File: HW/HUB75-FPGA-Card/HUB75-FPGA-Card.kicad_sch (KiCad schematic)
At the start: 0 parts

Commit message: add usb audio implementation
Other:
- added sheet USB Audio (USBAudio.kicad_sch)
- sheet FPGA ports: added B1, B2, B3, B4, BLANK, CLKOUT, CLK_12MHZ, CLK_60MHZ, D0, D1, D2, D3, D4, D5, D6, D7, G1, G2, G3, G4, LAT, R1, R2, R3, R4, ROW_CLK, ROW_DATA, STRIP1, STRIP2, STRIP3, STRIP4, ~{OE}, ~{RD}, ~{RXF}, ~{TXE}, ~{WR}; removed none
- sheet FTDI ports: added none; removed VIN_5V
- sheet Hub75 ports: added B1, B2, B3, B4, BLANK, CLKOUT, G1, G2, G3, G4, LAT, R1, R2, R3, R4, ROW_CLK, ROW_DATA, STRIP1, STRIP2, STRIP3, STRIP4; removed none

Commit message: rename Hub75 schematic page to LevelShifters
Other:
- sheet Hub75 renamed Level Shifters
- sheet Level Shifters: file Hub75.kicad_sch -> LevelShifters.kicad_sch
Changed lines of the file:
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@@
     (stroke (width 0.1524) (type solid))
     (fill (color 0 0 0 0.0000))
-    (property "Sheetname" "Hub75" (at 168.91 50.0884 0)
+    (property "Sheetname" "Level Shifters" (at 168.91 50.0884 0)
       (effects (font (size 1.27 1.27)) (justify left bottom))
     )
-    (property "Sheetfile" "Hub75.kicad_sch" (at 168.91 114.8846 0)
+    (property "Sheetfile" "LevelShifters.kicad_sch" (at 168.91 114.8846 0)
       (effects (font (size 1.27 1.27)) (justify left top))
     )

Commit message: finish up schematic and begin routing
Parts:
- added H1, H2, H3, H4: MountingHole, MountingHole:MountingHole_3.2mm_M3, symbol Mechanical:MountingHole
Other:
- removed sheet Power
- added sheet USB Hub (USBHub.kicad_sch)

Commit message: saving hardware progress
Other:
- added sheet MCU (MCU.kicad_sch)
- sheet USB Hub ports: added USB_MCU_D+, USB_MCU_D-; removed none

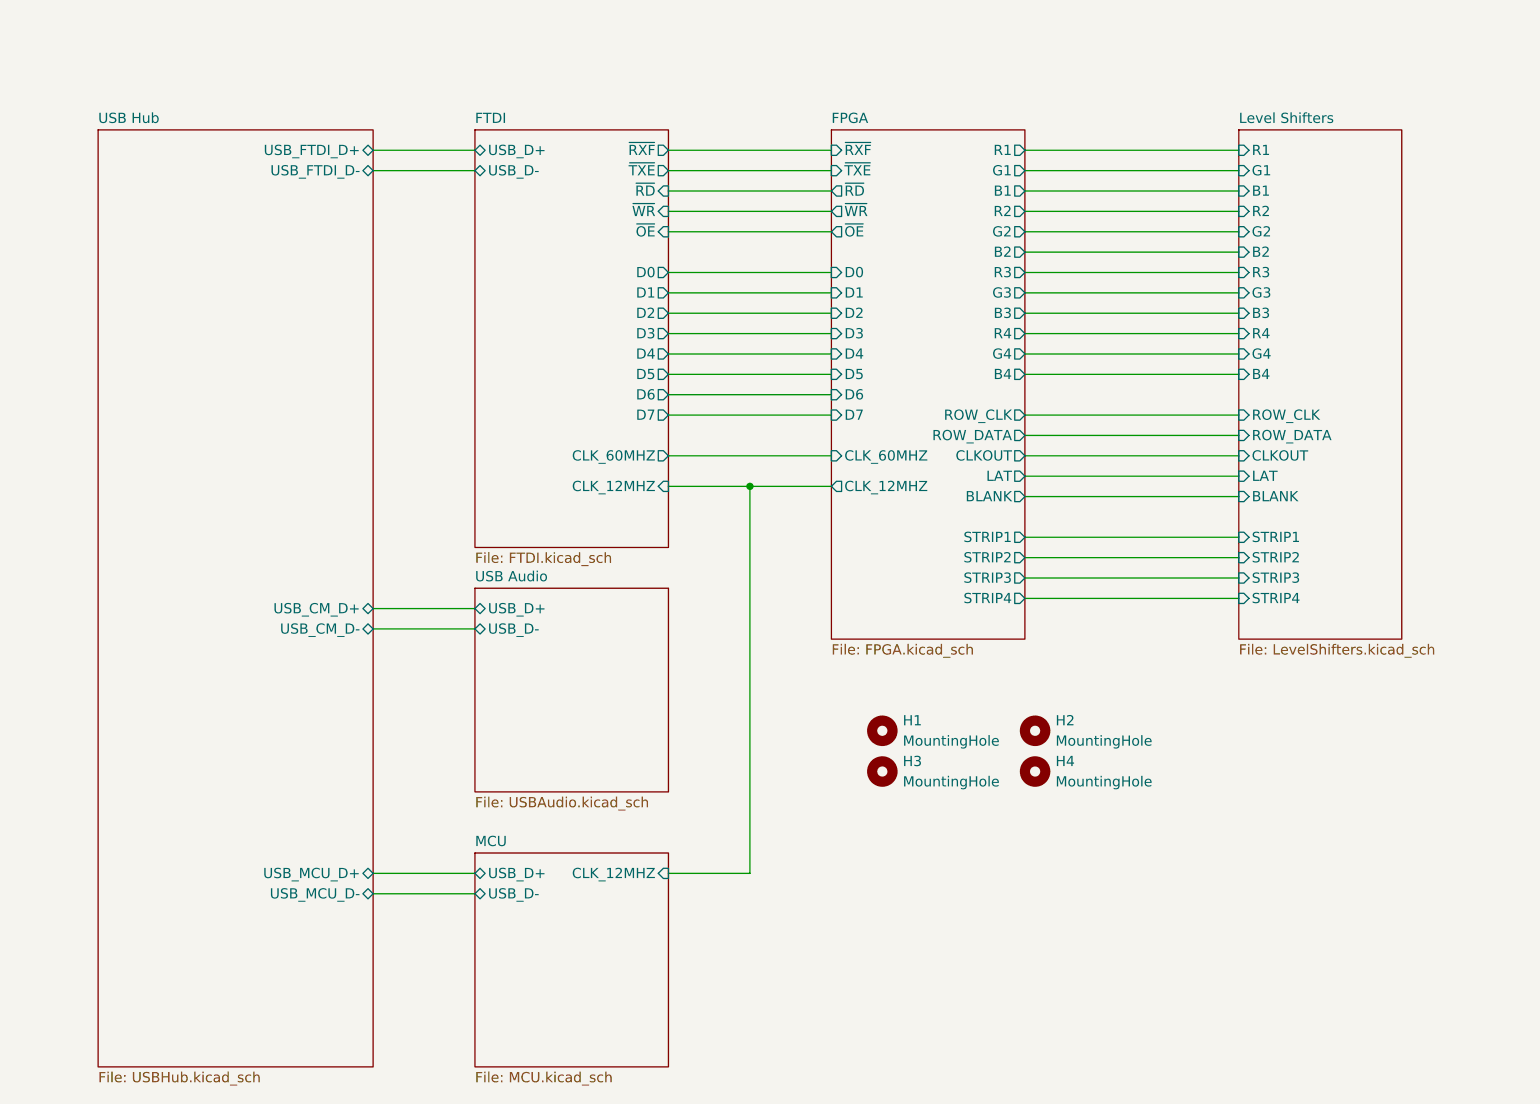
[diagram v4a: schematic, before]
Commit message: initial v1.1 board layout
still needs rp2040 pins routed
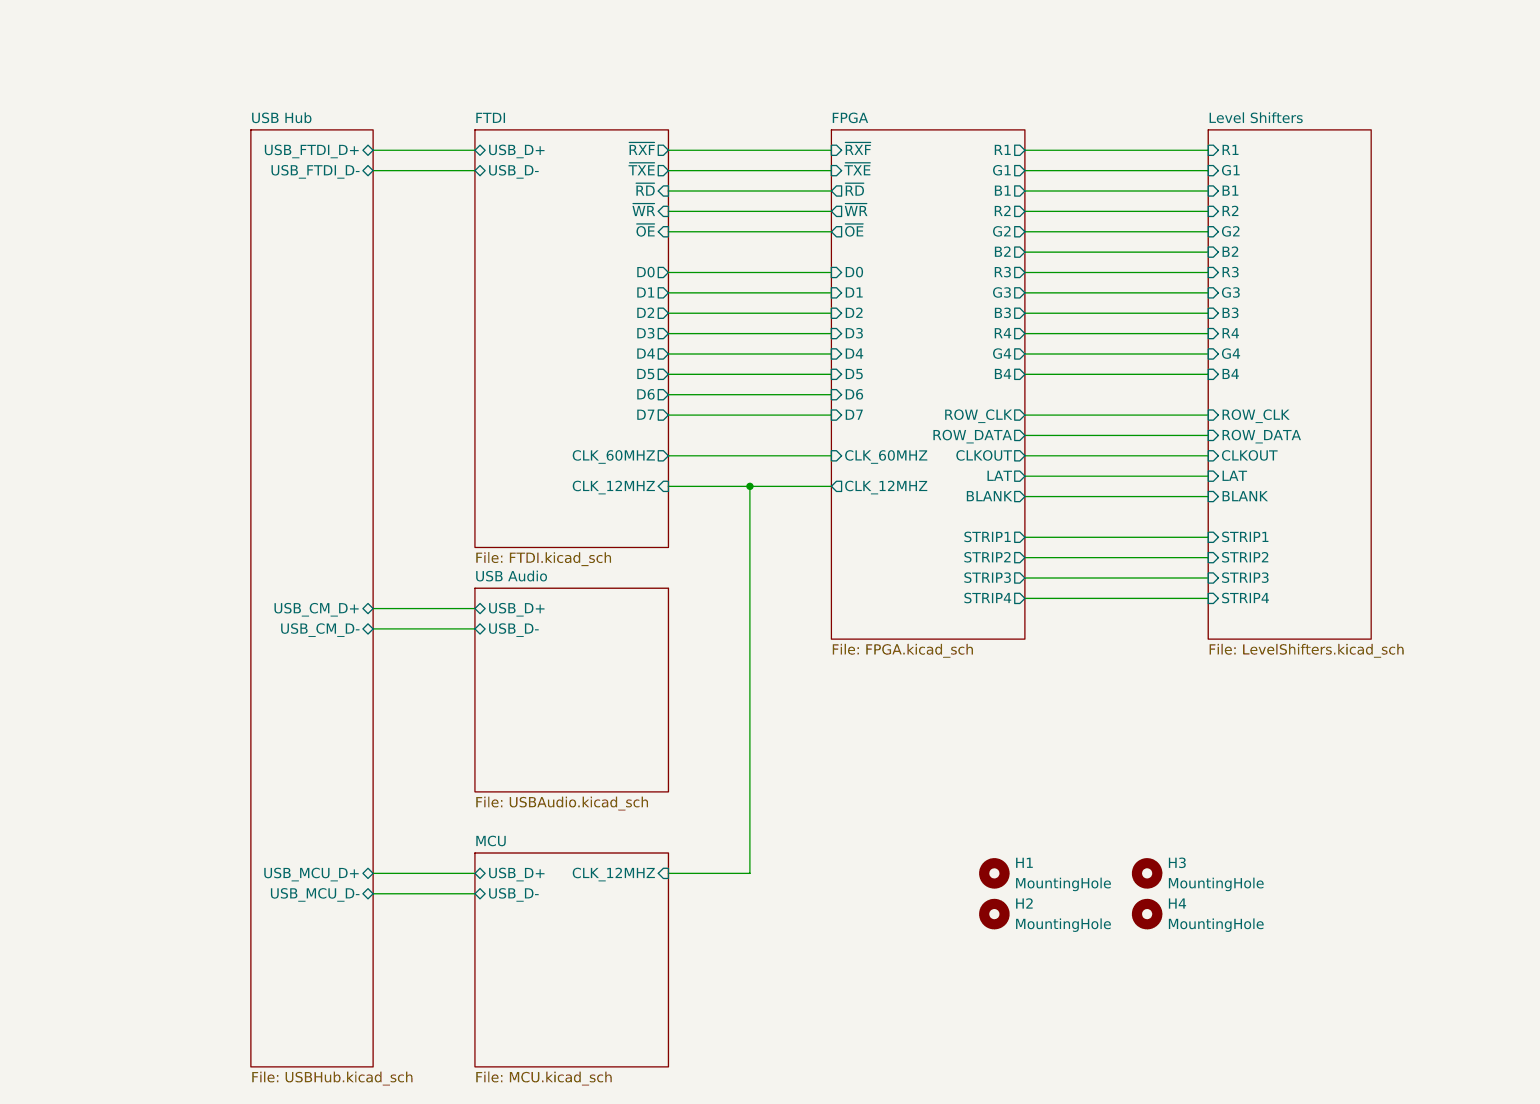
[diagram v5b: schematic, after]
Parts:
- renumbered H3 to H2, H2 to H3
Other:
- moved on the sheet: H1, H2, H3, H4

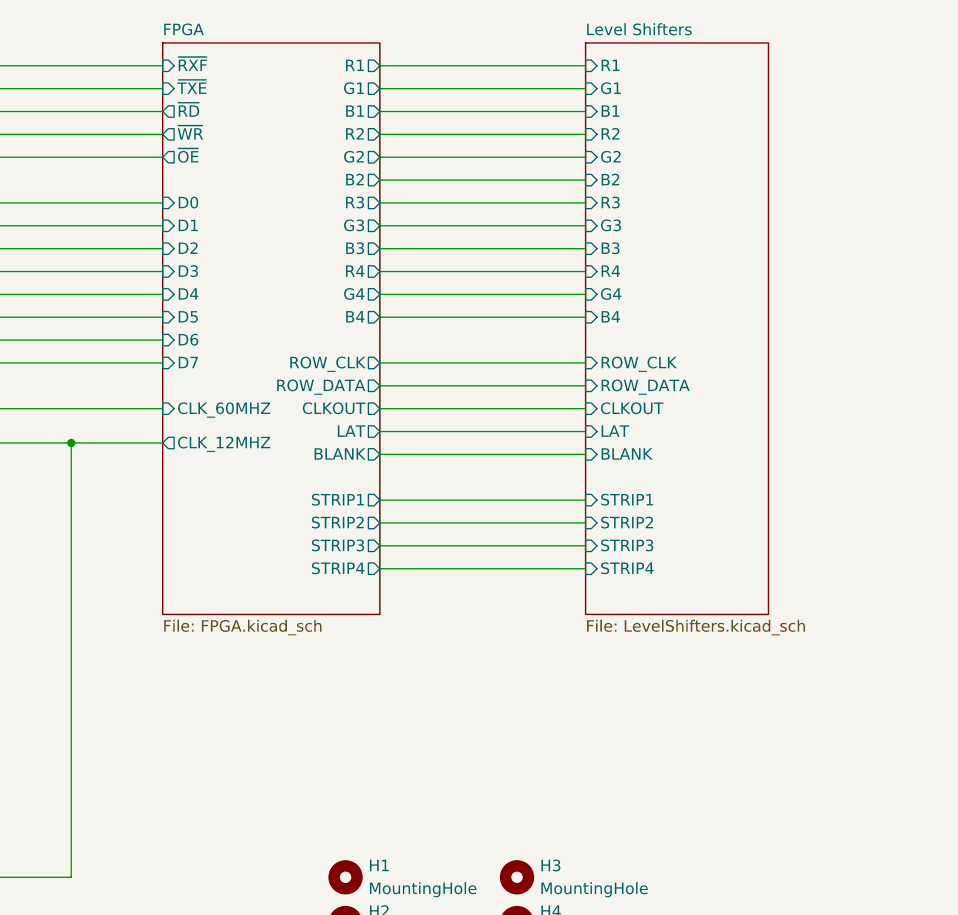
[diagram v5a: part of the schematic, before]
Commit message: update components and generate production files
still need to look into CBSEL
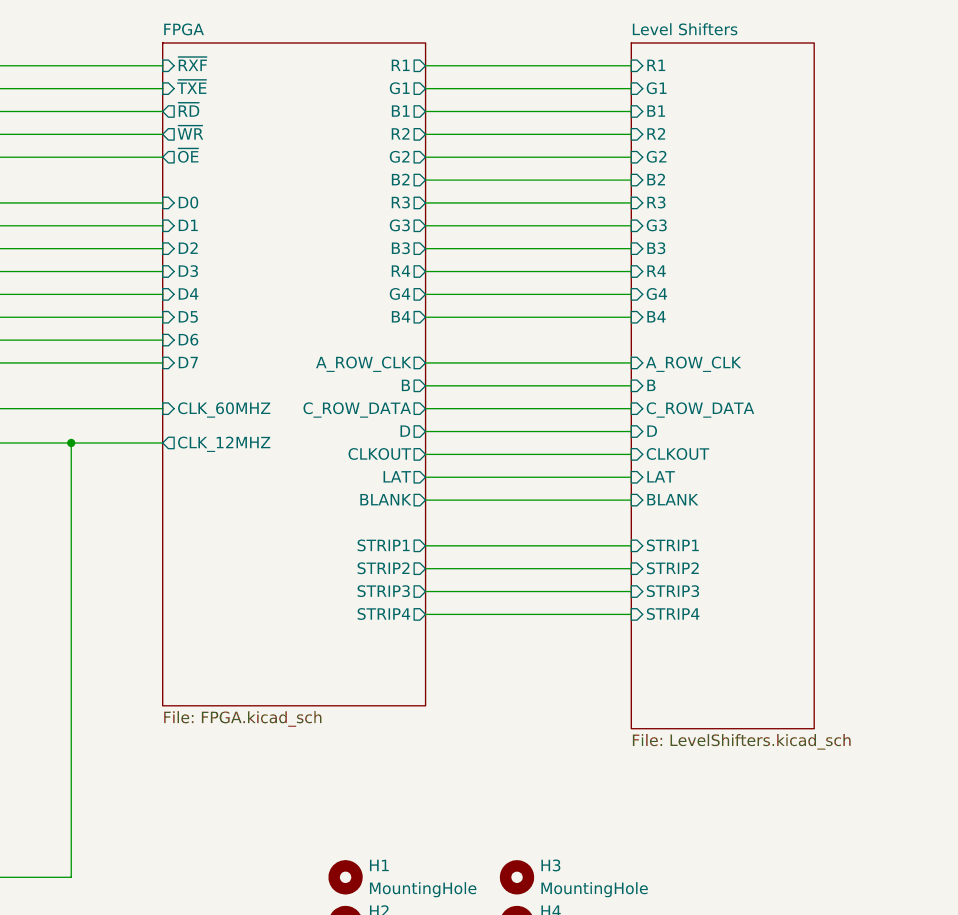
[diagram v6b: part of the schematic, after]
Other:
- sheet FPGA ports: added A_ROW_CLK, B, C_ROW_DATA, D; removed ROW_CLK, ROW_DATA
- sheet Level Shifters ports: added A_ROW_CLK, B, C_ROW_DATA, D; removed ROW_CLK, ROW_DATA
